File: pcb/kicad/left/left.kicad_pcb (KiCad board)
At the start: 2 copper layers, 135.9 x 89.9 mm, 61 parts, among them J1 USB_C_Receptacle_USB2.0, J2 AudioJack4, J3 Conn_01x12_Male, SW1 BOOT, SW10 SW_Push, SW12 SW_Push, SW13 SW_Push, SW14 SW_Push, SW15 SW_Push, SW17 SW_Push, SW18 SW_Push, SW19 SW_Push, SW2 RESET, SW21 SW_Push, SW22 SW_Push, SW23 SW_Push, SW24 SW_Push, SW3 SW_Push, SW31 SW_Push, SW32 SW_Push, SW33 SW_Push, SW34 SW_Push, SW4 SW_Push, SW5 SW_Push, SW7 SW_Push, SW8 SW_Push, SW9 SW_Push, U1 STM32, U2 LDO

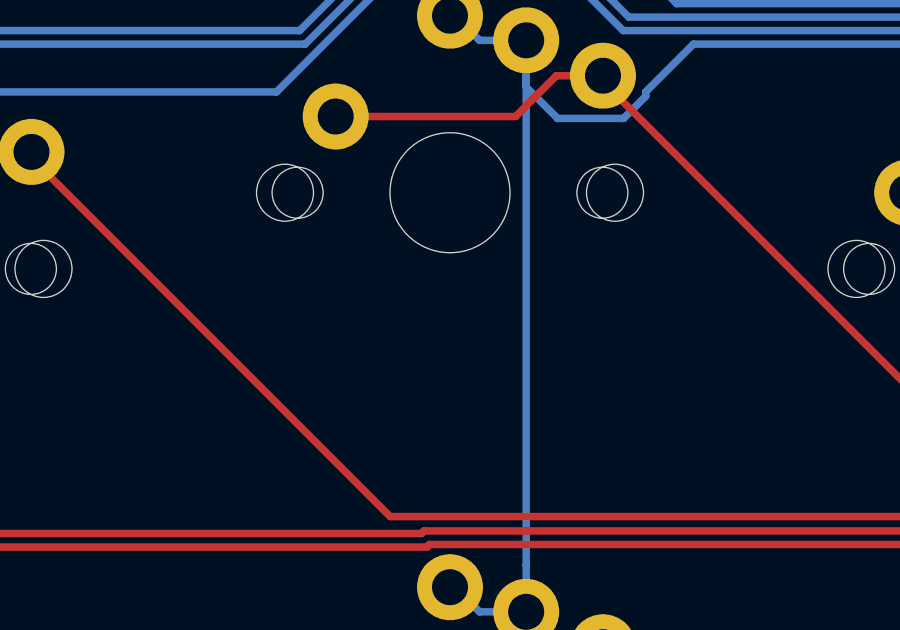
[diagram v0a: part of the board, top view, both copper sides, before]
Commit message: order number placeholder for JLPCB
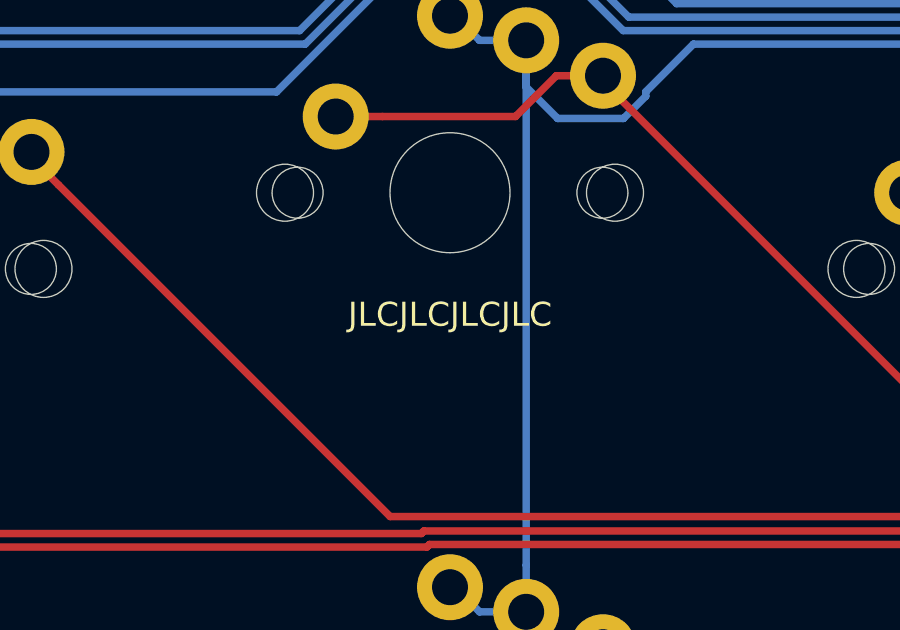
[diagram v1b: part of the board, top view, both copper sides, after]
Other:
- board text added: "JLCJLCJLCJLC"
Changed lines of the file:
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@@
   (general
     (thickness 1.6)
-    (drawings 24)
+    (drawings 25)
     (tracks 719)
     (zones 0)
@@
     )
   )
+  (gr_text JLCJLCJLCJLC (at 171.45 55.499) (layer F.SilkS)
+    (effects (font (size 0.8 0.8) (thickness 0.2)))
+  )
   (gr_text "KeySeeBee v0.1 by TeXitoi" (at 238.633 104.775 90) (layer F.SilkS)

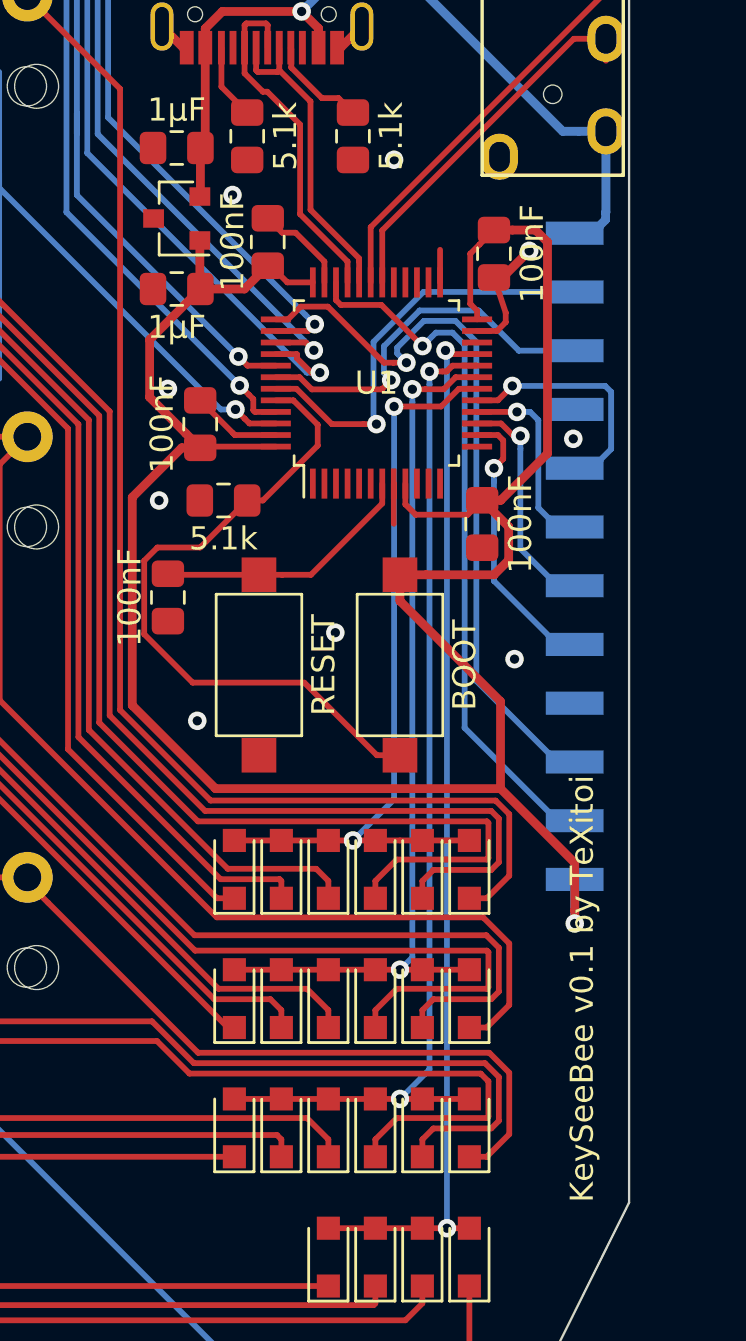
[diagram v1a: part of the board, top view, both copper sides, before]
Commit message: Fix LDO
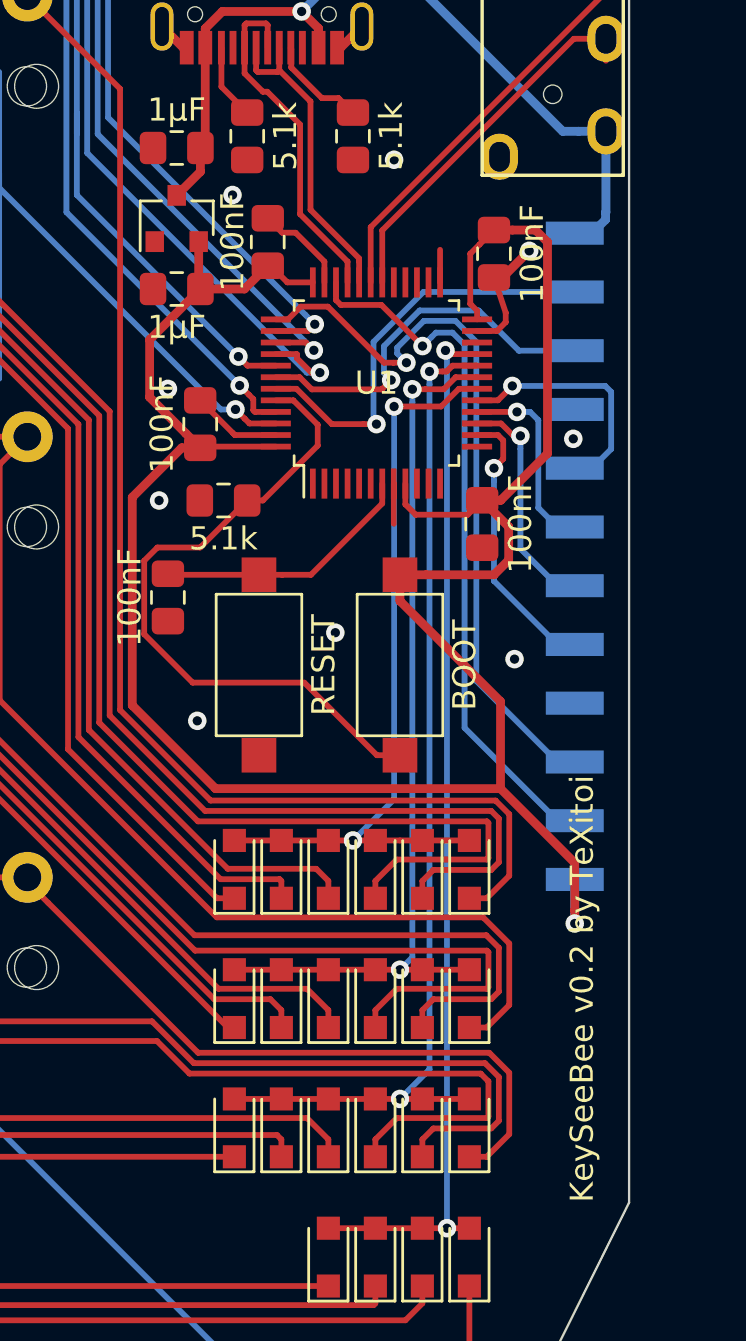
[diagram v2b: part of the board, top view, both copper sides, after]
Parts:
- turned U2 to 90 degrees
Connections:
- U2 pad 1: 3.3V -> GND
- U2 pad 2: 5V -> 3.3V
- U2 pad 3: GND -> 5V
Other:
- board text added: "KeySeeBee v0.2 by TeXitoi"
- board text removed: "KeySeeBee v0.1 by TeXitoi"
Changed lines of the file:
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@@
     (thickness 1.6)
     (drawings 25)
-    (tracks 719)
+    (tracks 718)
     (zones 0)
     (modules 61)
@@
   )
   (setup
-    (last_trace_width 0.25)
+    (last_trace_width 0.381)
     (user_trace_width 0.381)
     (trace_clearance 0.2)
@@
   )
   (module Package_TO_SOT_SMD:SOT-23 (layer F.Cu)
-    (at 221.107 62.23 180)
+    (at 221.107 62.23 90)
     (descr "SOT-23, Standard")
     (tags SOT-23)
     (attr smd)
-    (fp_text reference U2 (at 2.794 0.127 180) (layer F.SilkS) hide
-      (effects (font (size 1 1) (thickness 0.15)))
-    )
-    (fp_text value LDO (at 0 2.5 180) (layer F.Fab)
+    (fp_text reference U2 (at 2.794 0.127 90) (layer F.SilkS) hide
+      (effects (font (size 1 1) (thickness 0.15)))
+    )
+    (fp_text value LDO (at 0 2.5 90) (layer F.Fab)
       (effects (font (size 1 1) (thickness 0.15)))
     )
@@
     (fp_line (start -0.15 -1.52) (end 0.7 -1.52) (layer F.Fab) (width 0.1))
     (fp_line (start -0.7 -0.95) (end -0.7 1.5) (layer F.Fab) (width 0.1))
-    (fp_text user %R (at 0 0 270) (layer F.Fab)
+    (fp_text user %R (at 0 0 180) (layer F.Fab)
       (effects (font (size 0.5 0.5) (thickness 0.075)))
     )
-    (pad 3 smd rect (at 1 0 180) (size 0.9 0.8) (layers F.Cu F.Paste F.Mask)
+    (pad 3 smd rect (at 1 0 90) (size 0.9 0.8) (layers F.Cu F.Paste F.Mask)
+      (net 2 5V))
+    (pad 2 smd rect (at -1 0.95 90) (size 0.9 0.8) (layers F.Cu F.Paste F.Mask)
+      (net 10 3.3V))
+    (pad 1 smd rect (at -1 -0.95 90) (size 0.9 0.8) (layers F.Cu F.Paste F.Mask)
       (net 1 GND))
-    (pad 2 smd rect (at -1 0.95 180) (size 0.9 0.8) (layers F.Cu F.Paste F.Mask)
-      (net 2 5V))
-    (pad 1 smd rect (at -1 -0.95 180) (size 0.9 0.8) (layers F.Cu F.Paste F.Mask)
-      (net 10 3.3V))
     (model ${KISYS3DMOD}/Package_TO_SOT_SMD.3dshapes/SOT-23.wrl
       (at (xyz 0 0 0))
@@
     (effects (font (size 0.8 0.8) (thickness 0.2)))
   )
-  (gr_text "KeySeeBee v0.1 by TeXitoi" (at 238.633 104.775 90) (layer F.SilkS)
+  (gr_text "KeySeeBee v0.2 by TeXitoi" (at 238.633 104.775 90) (layer F.SilkS)
     (effects (font (size 1 1) (thickness 0.2)) (justify left))
   )
@@
   (segment (start 239.663 58.46) (end 239.663 61.962) (width 0.381) (layer B.Cu) (net 2))
   (segment (start 239.663 61.962) (end 239.649 61.976) (width 0.381) (layer B.Cu) (net 2))
-  (segment (start 222.34 58.974) (end 222.132 59.182) (width 0.381) (layer F.Cu) (net 2))
   (segment (start 222.34 54.845) (end 222.34 58.974) (width 0.381) (layer F.Cu) (net 2))
-  (segment (start 222.132 61.255) (end 222.107 61.28) (width 0.381) (layer F.Cu) (net 2))
-  (segment (start 222.132 59.182) (end 222.132 61.255) (width 0.381) (layer F.Cu) (net 2))
+  (segment (start 222.132 60.205) (end 221.107 61.23) (width 0.381) (layer F.Cu) (net 2))
+  (segment (start 222.132 59.182) (end 222.132 60.205) (width 0.381) (layer F.Cu) (net 2))
   (segment (start 226.06 54.904) (end 226.06 55.70359) (width 0.25) (layer F.Cu) (net 4))
   (segment (start 226.04 54.845) (end 226.04 54.884) (width 0.25) (layer F.Cu) (net 4))
@@
   (segment (start 225.171 64.271) (end 225.053 64.389) (width 0.25) (layer F.Cu) (net 10))
   (via (at 238.315 92.71) (size 0.8) (drill 0.4) (layers F.Cu B.Cu) (net 10))
-  (segment (start 222.107 65.253) (end 222.132 65.278) (width 0.381) (layer F.Cu) (net 10))
-  (segment (start 222.107 63.18) (end 222.107 65.253) (width 0.381) (layer F.Cu) (net 10))
   (segment (start 224.037 65.278) (end 225.044 64.271) (width 0.381) (layer F.Cu) (net 10))
   (segment (start 222.132 65.278) (end 224.037 65.278) (width 0.381) (layer F.Cu) (net 10))
@@
   (segment (start 234.315 74.413) (end 235.115 74.413) (width 0.381) (layer F.Cu) (net 10))
   (segment (start 238.315 92.71) (end 238.315 90.805) (width 0.381) (layer B.Cu) (net 10))
+  (segment (start 222.057 65.203) (end 222.132 65.278) (width 0.381) (layer F.Cu) (net 10))
+  (segment (start 222.057 63.23) (end 222.057 65.203) (width 0.381) (layer F.Cu) (net 10))
   (segment (start 225.663 77.634) (end 224.663 77.634) (width 0.25) (layer F.Cu) (net 14))
   (segment (start 226.911002 77.634) (end 225.663 77.634) (width 0.25) (layer F.Cu) (net 14))

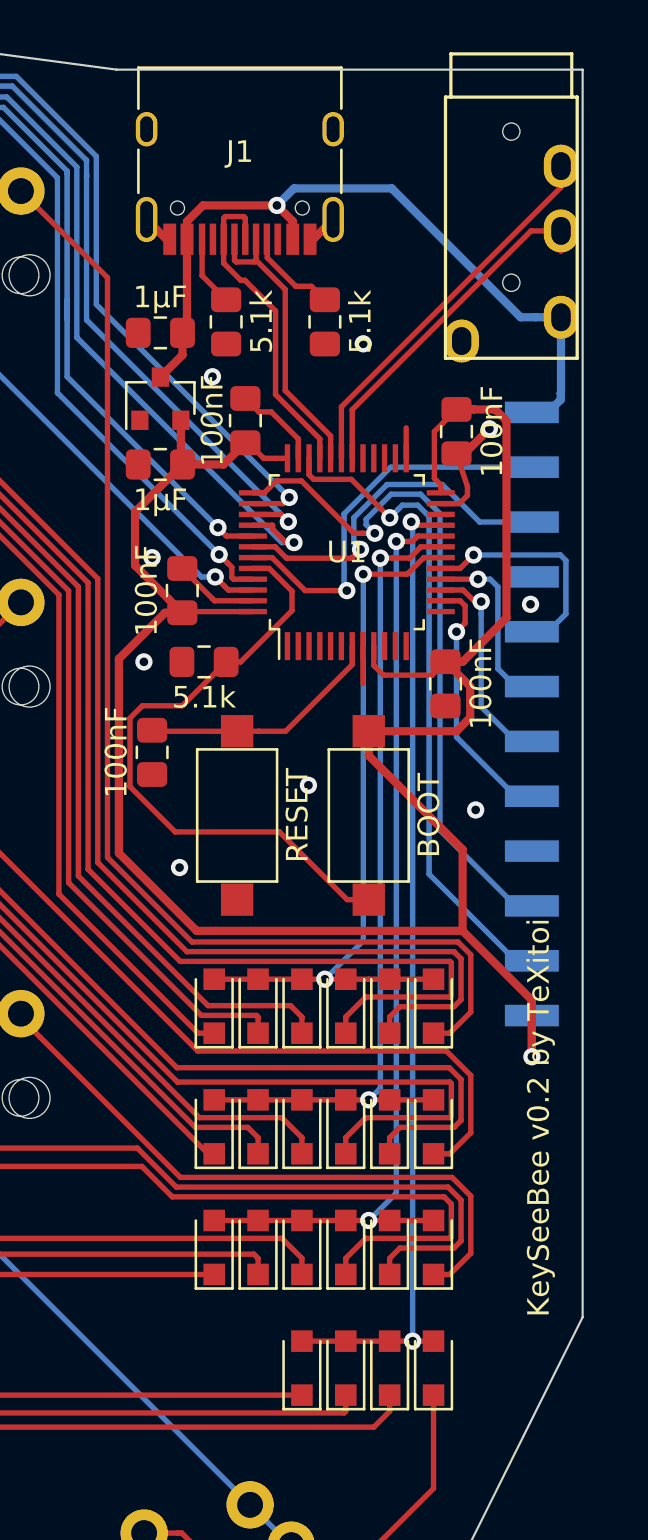
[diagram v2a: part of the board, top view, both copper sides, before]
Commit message: Fix diode orientation
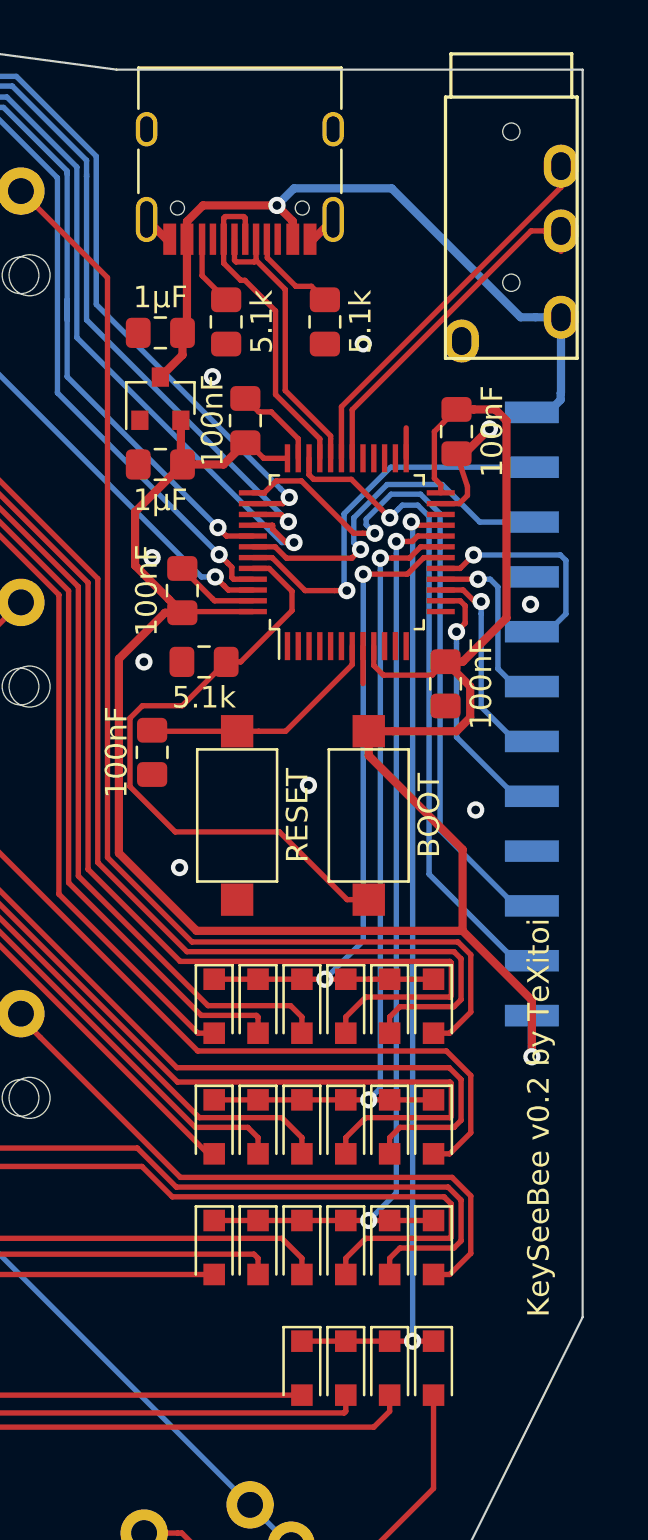
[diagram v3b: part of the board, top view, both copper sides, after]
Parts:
- turned D10 to 270 degrees
- turned D11 to 270 degrees
- turned D12 to 270 degrees
- turned D14 to 270 degrees
- turned D15 to 270 degrees
- turned D16 to 270 degrees
- turned D17 to 270 degrees
- turned D19 to 270 degrees
- turned D20 to 270 degrees
- turned D21 to 270 degrees
- turned D23 to 270 degrees
- turned D24 to 270 degrees
- turned D25 to 270 degrees
- turned D26 to 270 degrees
- turned D33 to 270 degrees
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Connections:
- D10 pad 1: Net-(D10-Pad1) -> ROW2
- D10 pad 2: ROW2 -> Net-(D10-Pad2)
- D11 pad 1: Net-(D11-Pad1) -> ROW3
- D11 pad 2: ROW3 -> Net-(D11-Pad2)
- D12 pad 1: Net-(D12-Pad1) -> ROW4
- D12 pad 2: ROW4 -> Net-(D12-Pad2)
- D14 pad 1: Net-(D14-Pad1) -> ROW1
- D14 pad 2: ROW1 -> Net-(D14-Pad2)
- D15 pad 1: Net-(D15-Pad1) -> ROW2
- D15 pad 2: ROW2 -> Net-(D15-Pad2)
- D16 pad 1: Net-(D16-Pad1) -> ROW3
- D16 pad 2: ROW3 -> Net-(D16-Pad2)
- D17 pad 1: Net-(D17-Pad1) -> ROW4
- D17 pad 2: ROW4 -> Net-(D17-Pad2)
- D19 pad 1: Net-(D19-Pad1) -> ROW1
- D19 pad 2: ROW1 -> Net-(D19-Pad2)
- D20 pad 1: Net-(D20-Pad1) -> ROW2
- D20 pad 2: ROW2 -> Net-(D20-Pad2)
- D21 pad 1: Net-(D21-Pad1) -> ROW3
- D21 pad 2: ROW3 -> Net-(D21-Pad2)
- D23 pad 1: Net-(D23-Pad1) -> ROW1
- D23 pad 2: ROW1 -> Net-(D23-Pad2)
- D24 pad 1: Net-(D24-Pad1) -> ROW2
- D24 pad 2: ROW2 -> Net-(D24-Pad2)
- D25 pad 1: Net-(D25-Pad1) -> ROW3
- D25 pad 2: ROW3 -> Net-(D25-Pad2)
- D26 pad 1: Net-(D26-Pad1) -> ROW4
- D26 pad 2: ROW4 -> Net-(D26-Pad2)
- D33 pad 1: Net-(D33-Pad1) -> ROW1
- D33 pad 2: ROW1 -> Net-(D33-Pad2)
- D34 pad 1: Net-(D34-Pad1) -> ROW2
- D34 pad 2: ROW2 -> Net-(D34-Pad2)
- D35 pad 1: Net-(D35-Pad1) -> ROW3
- D35 pad 2: ROW3 -> Net-(D35-Pad2)
- D36 pad 1: Net-(D36-Pad1) -> ROW4
- D36 pad 2: ROW4 -> Net-(D36-Pad2)
- D5 pad 1: Net-(D5-Pad1) -> ROW1
- D5 pad 2: ROW1 -> Net-(D5-Pad2)
- D6 pad 1: Net-(D6-Pad1) -> ROW2
- D6 pad 2: ROW2 -> Net-(D6-Pad2)
- D7 pad 1: Net-(D7-Pad1) -> ROW3
- D7 pad 2: ROW3 -> Net-(D7-Pad2)
- D9 pad 1: Net-(D9-Pad1) -> ROW1
- D9 pad 2: ROW1 -> Net-(D9-Pad2)
- SW10 pad 1: Net-(D12-Pad1) -> Net-(D12-Pad2)
- SW12 pad 1: Net-(D14-Pad1) -> Net-(D14-Pad2)
- SW13 pad 1: Net-(D15-Pad1) -> Net-(D15-Pad2)
- SW14 pad 1: Net-(D16-Pad1) -> Net-(D16-Pad2)
- SW15 pad 1: Net-(D17-Pad1) -> Net-(D17-Pad2)
- SW17 pad 1: Net-(D19-Pad1) -> Net-(D19-Pad2)
- SW18 pad 1: Net-(D20-Pad1) -> Net-(D20-Pad2)
- SW19 pad 1: Net-(D21-Pad1) -> Net-(D21-Pad2)
- SW21 pad 1: Net-(D23-Pad1) -> Net-(D23-Pad2)
- SW22 pad 1: Net-(D24-Pad1) -> Net-(D24-Pad2)
- SW23 pad 1: Net-(D25-Pad1) -> Net-(D25-Pad2)
- SW24 pad 1: Net-(D26-Pad1) -> Net-(D26-Pad2)
- SW3 pad 1: Net-(D5-Pad1) -> Net-(D5-Pad2)
- SW31 pad 1: Net-(D33-Pad1) -> Net-(D33-Pad2)
- SW32 pad 1: Net-(D34-Pad1) -> Net-(D34-Pad2)
- SW33 pad 1: Net-(D35-Pad1) -> Net-(D35-Pad2)
- SW34 pad 1: Net-(D36-Pad1) -> Net-(D36-Pad2)
- SW4 pad 1: Net-(D6-Pad1) -> Net-(D6-Pad2)
- SW5 pad 1: Net-(D7-Pad1) -> Net-(D7-Pad2)
- SW7 pad 1: Net-(D9-Pad1) -> Net-(D9-Pad2)
- SW8 pad 1: Net-(D10-Pad1) -> Net-(D10-Pad2)
- SW9 pad 1: Net-(D11-Pad1) -> Net-(D11-Pad2)
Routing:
- net Net-(D5-Pad2): track 0.00 -> 136.6 mm
- net Net-(D5-Pad1): track 136.6 -> 0.00 mm
- net Net-(D6-Pad2): track 0.00 -> 122.8 mm
- net Net-(D6-Pad1): track 122.8 -> 0.00 mm
- net Net-(D19-Pad2): track 0.00 -> 118.1 mm
- net Net-(D19-Pad1): track 118.1 -> 0.00 mm
- net Net-(D7-Pad2): track 0.00 -> 116.8 mm
- net Net-(D7-Pad1): track 116.8 -> 0.00 mm
- net Net-(D9-Pad2): track 0.00 -> 105.2 mm
- net Net-(D9-Pad1): track 105.2 -> 0.00 mm
- net Net-(D20-Pad2): track 0.00 -> 104.6 mm
- net Net-(D20-Pad1): track 104.6 -> 0.00 mm
- net Net-(D23-Pad2): track 0.00 -> 99.9 mm
- net Net-(D23-Pad1): track 99.9 -> 0.00 mm
- net Net-(D21-Pad2): track 0.00 -> 99.0 mm
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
